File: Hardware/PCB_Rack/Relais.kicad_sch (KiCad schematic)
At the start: 5 parts, among them Q1 IRLML6244, Q2 IRLML6244

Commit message: check schematic pcb
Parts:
- added J2: Conn_01x03, symbol Connector_Generic:Conn_01x03
- renumbered R7 to R, U3 to U
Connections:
- net GND: now also J2.3 (Pin_3)
- net Entree1+: no longer names the net of U.4 (O11), U.5 (O12)
- net Entree1+: now also J2.1 (Pin_1)
- net Entree1- renamed VAC
- net INA1_1 renamed RESET
- net INA1_2 renamed SET
- new net NEUT: J2.2 (Pin_2)

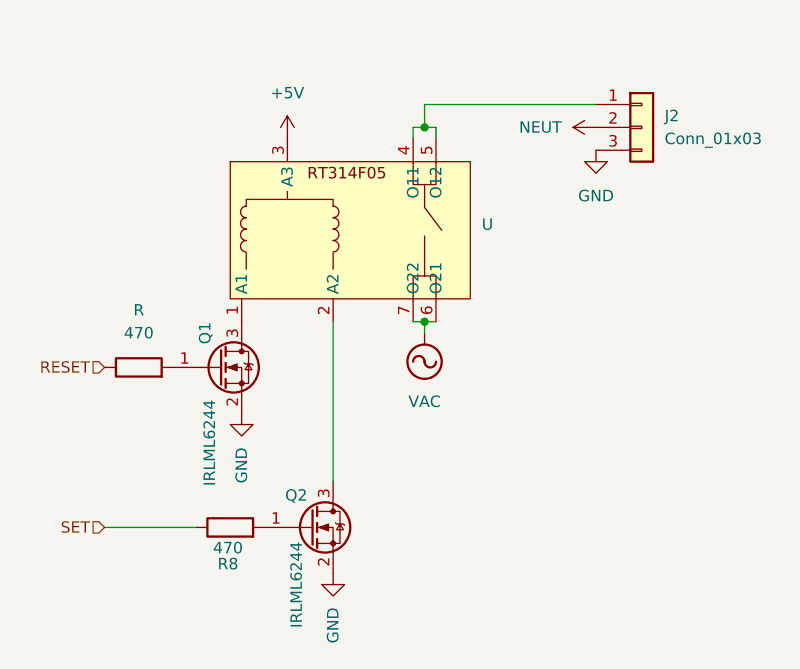
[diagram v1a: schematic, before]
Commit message: finalisation schematic PCB RACK + modif README
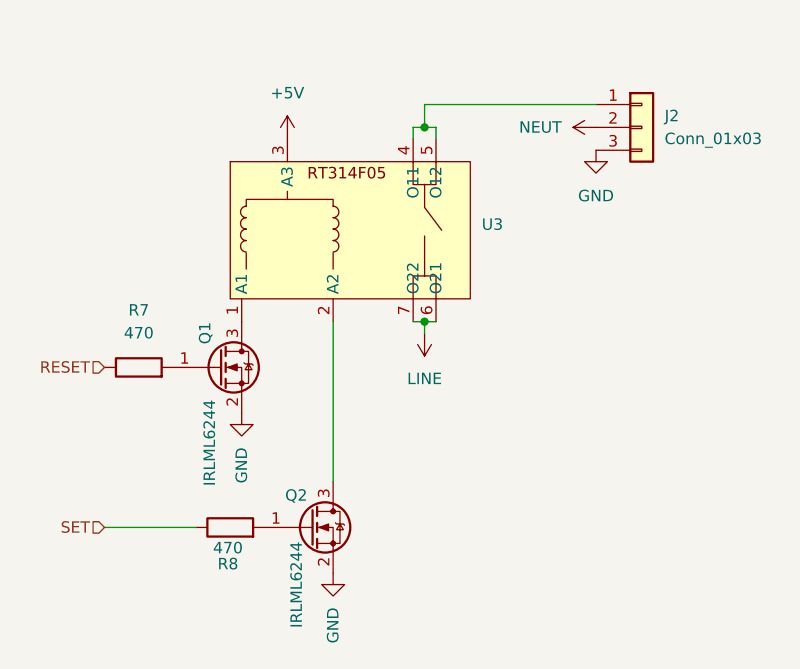
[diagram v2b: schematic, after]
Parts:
- U3: renamed from U; footprint (none) -> Relais_Bistable_SPDT:SPDT_bistable; MPN (none) -> 8-1393239-5
- renumbered R to R7
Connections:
- net VAC renamed LINE
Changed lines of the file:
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@@
-	)
-	(symbol
-		(lib_id "power:VAC")
-		(at 158.75 82.55 180)
-		(unit 1)
-		(exclude_from_sim no)
-		(in_bom yes)
-		(on_board yes)
-		(dnp no)
-		(fields_autoplaced yes)
-		(property "Reference" "#PWR0201"
-			(at 158.75 80.01 0)
-			(effects
-				(font
-					(size 1.27 1.27)
-				)
-				(hide yes)
-			)
-		)
-		(property "Value" "VAC"
-			(at 158.75 90.17 0)
-			(effects
-				(font
-					(size 1.27 1.27)
-				)
-			)
-		)
-		(property "Footprint" ""
-			(at 158.75 82.55 0)
-			(effects
-				(font
-					(size 1.27 1.27)
-				)
-				(hide yes)
-			)
-		)
-		(property "Datasheet" ""
-			(at 158.75 82.55 0)
-			(effects
-				(font
-					(size 1.27 1.27)
-				)
-				(hide yes)
-			)
-		)
-		(property "Description" "Power symbol creates a global label with name \"VAC\""
-			(at 158.75 82.55 0)
-			(effects
-				(font
-					(size 1.27 1.27)
-				)
-				(hide yes)
-			)
-		)
-		(pin "1"
-		)
-		(instances
-			(project ""
-				(path "/24795ffd-bac6-477a-a38e-d8501482d995/5442e838-22b7-4759-82c9-b29dca855bd1"
-					(reference "#PWR0201")
-					(unit 1)
-				)
-				(path "/24795ffd-bac6-477a-a38e-d8501482d995/5e4c1706-e559-4546-9182-b23e927581d6"
-					(reference "#PWR0316")
-					(unit 1)
-				)
-				(path "/24795ffd-bac6-477a-a38e-d8501482d995/75b15100-946d-4ab0-a7ee-fd42b4c9e313"
-					(reference "#PWR0310")
-					(unit 1)
-				)
-				(path "/24795ffd-bac6-477a-a38e-d8501482d995/8b3a903d-fead-4375-b5bf-423b54a60210"
-					(reference "#PWR0304")
-					(unit 1)
-				)
-				(path "/24795ffd-bac6-477a-a38e-d8501482d995/b42fd1b5-6c7b-4805-bf9d-9efb210f2cb8"
-					(reference "#PWR0322")
-					(unit 1)
-				)
-				(path "/24795ffd-bac6-477a-a38e-d8501482d995/d6311d45-f513-4dac-bbb5-f801c07c799f"
-					(reference "#PWR0704")
-					(unit 1)
-				)
-			)
-		)
 	)
 	(symbol
@@
 		(dnp no)
 		(fields_autoplaced yes)
-		(property "Reference" "R"
+		(property "Reference" "R7"
 			(at 127 80.01 90)
 			(effects
@@
 		(instances
 			(project "PCB_Rack"
+				(path "/24795ffd-bac6-477a-a38e-d8501482d995/5442e838-22b7-4759-82c9-b29dca855bd1"
+					(reference "R7")
+					(unit 1)
+				)
 				(path "/24795ffd-bac6-477a-a38e-d8501482d995/5e4c1706-e559-4546-9182-b23e927581d6"
 					(reference "R305")
@@
 	)
 	(symbol
+		(lib_id "power:LINE")
+		(at 158.75 82.55 180)
+		(unit 1)
+		(exclude_from_sim no)
+		(in_bom yes)
+		(on_board yes)
+		(dnp no)
+		(fields_autoplaced yes)
+		(property "Reference" "#PWR01"
+			(at 158.75 78.74 0)
+			(effects
+				(font
+					(size 1.27 1.27)
+				)
+				(hide yes)
+			)
+		)
+		(property "Value" "LINE"
+			(at 158.75 87.63 0)
+			(effects
+				(font
+					(size 1.27 1.27)
+				)
+			)
+		)
+		(property "Footprint" ""
+			(at 158.75 82.55 0)
+			(effects
+				(font
+					(size 1.27 1.27)
+				)
+				(hide yes)
+			)
+		)
+		(property "Datasheet" ""
+			(at 158.75 82.55 0)
+			(effects
+				(font
+					(size 1.27 1.27)
+				)
+				(hide yes)
+			)
+		)
+		(property "Description" "Power symbol creates a global label with name \"LINE\""
+			(at 158.75 82.55 0)
+			(effects
+				(font
+					(size 1.27 1.27)
+				)
+				(hide yes)
+			)
+		)
+		(pin "1"
+		)
+		(instances
+			(project "PCB_Rack"
+				(path "/24795ffd-bac6-477a-a38e-d8501482d995/5442e838-22b7-4759-82c9-b29dca855bd1"
+					(reference "#PWR01")
+					(unit 1)
+				)
+				(path "/24795ffd-bac6-477a-a38e-d8501482d995/5e4c1706-e559-4546-9182-b23e927581d6"
+					(reference "#PWR030")
+					(unit 1)
+				)
+				(path "/24795ffd-bac6-477a-a38e-d8501482d995/75b15100-946d-4ab0-a7ee-fd42b4c9e313"
+					(reference "#PWR029")
+					(unit 1)
+				)
+				(path "/24795ffd-bac6-477a-a38e-d8501482d995/8b3a903d-fead-4375-b5bf-423b54a60210"
+					(reference "#PWR028")
+					(unit 1)
+				)
+				(path "/24795ffd-bac6-477a-a38e-d8501482d995/b42fd1b5-6c7b-4805-bf9d-9efb210f2cb8"
+					(reference "#PWR031")
+					(unit 1)
+				)
+				(path "/24795ffd-bac6-477a-a38e-d8501482d995/d6311d45-f513-4dac-bbb5-f801c07c799f"
+					(reference "#PWR032")
+					(unit 1)
+				)
+			)
+		)
+	)
+	(symbol
 		(lib_id "RT1_bistable:RT314F05_1")
 		(at 154.94 71.12 0)
@@
 		(dnp no)
 		(fields_autoplaced yes)
-		(property "Reference" "U"
+		(property "Reference" "U3"
 			(at 165.1 70.4849 0)
 			(effects
@@
 			)
 		)
-		(property "Footprint" ""
+		(property "Footprint" "Relais_Bistable_SPDT:SPDT_bistable"
 			(at 154.94 71.12 0)
 			(effects
@@
 			)
 		)
-		(property "Datasheet" ""
+		(property "Datasheet" "https://eu.mouser.com/datasheet/2/418/5/ENG_DS_RT1_bistable_0819-728100.pdf"
 			(at 154.94 71.12 0)
 			(effects
@@
 			)
 		)
-		(property "Description" ""
+		(property "Description" "General Purpose Relay Polarized bistable version with  2 coils SPDT"
 			(at 154.94 71.12 0)
 			(effects
@@
 			)
 		)
+		(property "MPN" "8-1393239-5"
+			(at 154.94 71.12 0)
+			(effects
+				(font
+					(size 1.27 1.27)
+				)
+				(hide yes)
+			)
+		)
 		(pin "5"
 		)
@@
 		(instances
 			(project "PCB_Rack"
+				(path "/24795ffd-bac6-477a-a38e-d8501482d995/5442e838-22b7-4759-82c9-b29dca855bd1"
+					(reference "U3")
+					(unit 1)
+				)
 				(path "/24795ffd-bac6-477a-a38e-d8501482d995/5e4c1706-e559-4546-9182-b23e927581d6"
 					(reference "U303")

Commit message: modif footprint + symbole module AC-DC
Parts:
- J2: footprint (none) -> Conn_Alim:Conn_Secteur
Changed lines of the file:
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@@
 			)
 		)
-		(property "Footprint" ""
+		(property "Footprint" "Conn_Alim:Conn_Secteur"
 			(at 182.88 59.69 0)
 			(effects

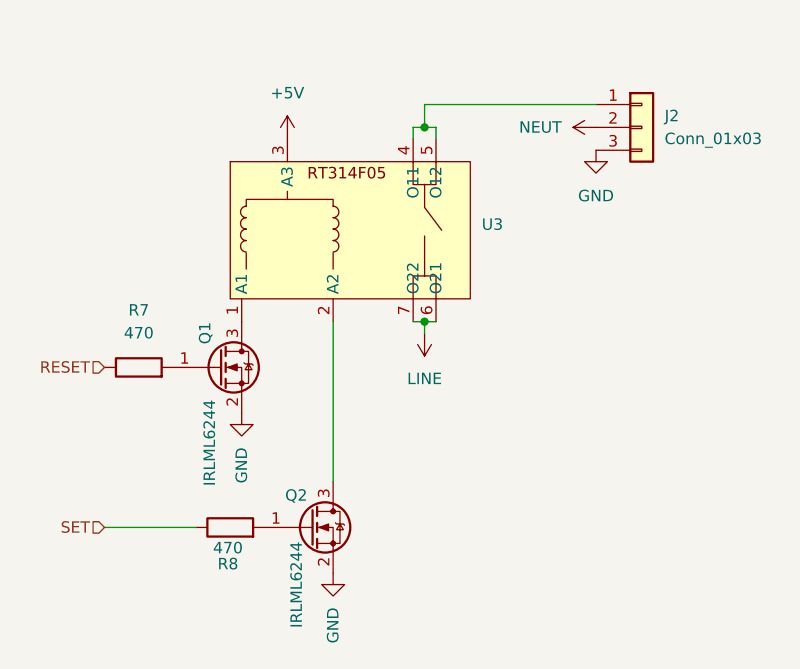
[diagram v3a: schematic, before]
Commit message: finalisation 2.0 schematic PCB RACK et début PCB
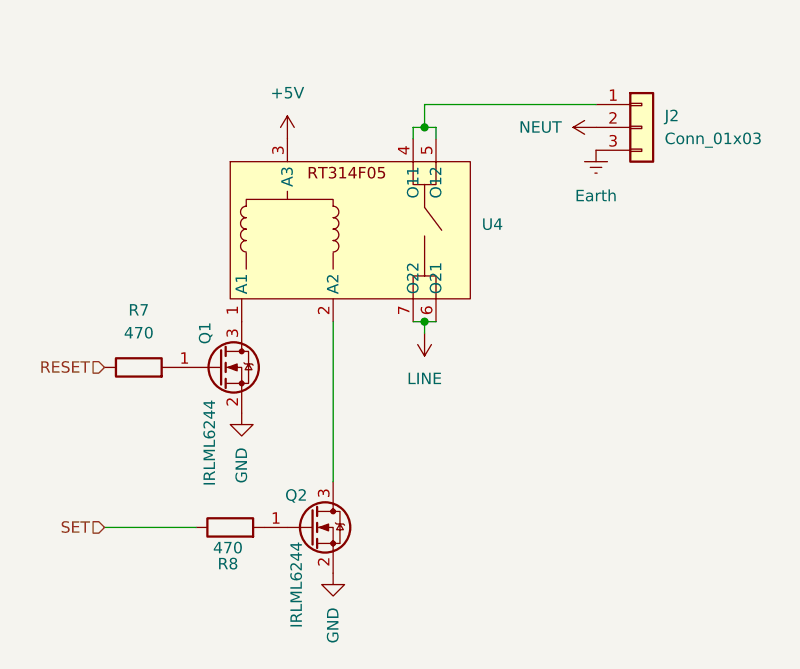
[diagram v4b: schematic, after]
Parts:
- renumbered U3 to U4
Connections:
- net GND: no longer J2.3 (Pin_3)
- new net Earth: J2.3 (Pin_3)

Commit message: finalisation PCB Rack
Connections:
- net LINE_Sw: now reaches J2.1 (Pin_1), U4.4 (O11), U4.5 (O12)
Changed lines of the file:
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@@
+		)
+	)
+	(label "LINE_Sw"
+		(at 158.75 57.15 0)
+		(effects
+			(font
+				(size 1.27 1.27)
+			)
+			(justify left bottom)
 		)
 	)

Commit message: update LOGO
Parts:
- Q1, Q2: value IRLML6244 -> SQ2310ES-T1_BE3; MPN (none) -> SQ2310ES
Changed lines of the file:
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@@
 			)
 		)
-		(property "Value" "IRLML6244"
-			(at 144.526 115.316 90)
+		(property "Value" "SQ2310ES-T1_BE3"
+			(at 153.924 113.284 90)
 			(effects
 				(font
@@
 			)
 		)
-		(property "Datasheet" "https://www.infineon.com/dgdl/Infineon-IRLML6244-DataSheet-v01_01-EN.pdf?fileId=5546d462533600a4015356686fed261f"
+		(property "Datasheet" "https://www.vishay.com/docs/67036/sq2310es.pdf"
 			(at 151.13 107.95 0)
 			(effects
@@
 		)
 		(property "Description" "6.3A Id, 20V Vds, 21mOhm Rds, N-Channel StrongIRFET Power MOSFET, SOT-23"
+			(at 146.05 104.14 0)
+			(effects
+				(font
+					(size 1.27 1.27)
+				)
+				(hide yes)
+			)
+		)
+		(property "MPN" "SQ2310ES"
+			(at 146.05 104.14 0)
+			(effects
+				(font
+					(size 1.27 1.27)
+				)
+				(hide yes)
+			)
+		)
+		(property "Field6" ""
 			(at 146.05 104.14 0)
 			(effects
@@
 			)
 		)
-		(property "Value" "IRLML6244"
-			(at 134.874 94.742 90)
+		(property "Value" "SQ2310ES-T1_BE3"
+			(at 141.986 88.138 90)
 			(effects
 				(font
@@
 			)
 		)
-		(property "Datasheet" "https://www.infineon.com/dgdl/Infineon-IRLML6244-DataSheet-v01_01-EN.pdf?fileId=5546d462533600a4015356686fed261f"
+		(property "Datasheet" "https://www.vishay.com/docs/67036/sq2310es.pdf"
 			(at 140.97 90.17 0)
 			(effects
@@
 			(effects
 				(font
+					(size 1.27 1.27)
+				)
+				(hide yes)
+			)
+		)
+		(property "MPN" "SQ2310ES"
+			(at 135.89 86.36 90)
+			(effects
+				(font
